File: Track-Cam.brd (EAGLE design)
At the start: 65 x 56 mm, 40 parts, among them IC1 STM32F042KT/M, IC2 BD6211F/M, IC3 BD6211F/M, X1 RASPI_BOARD_B+#_HC

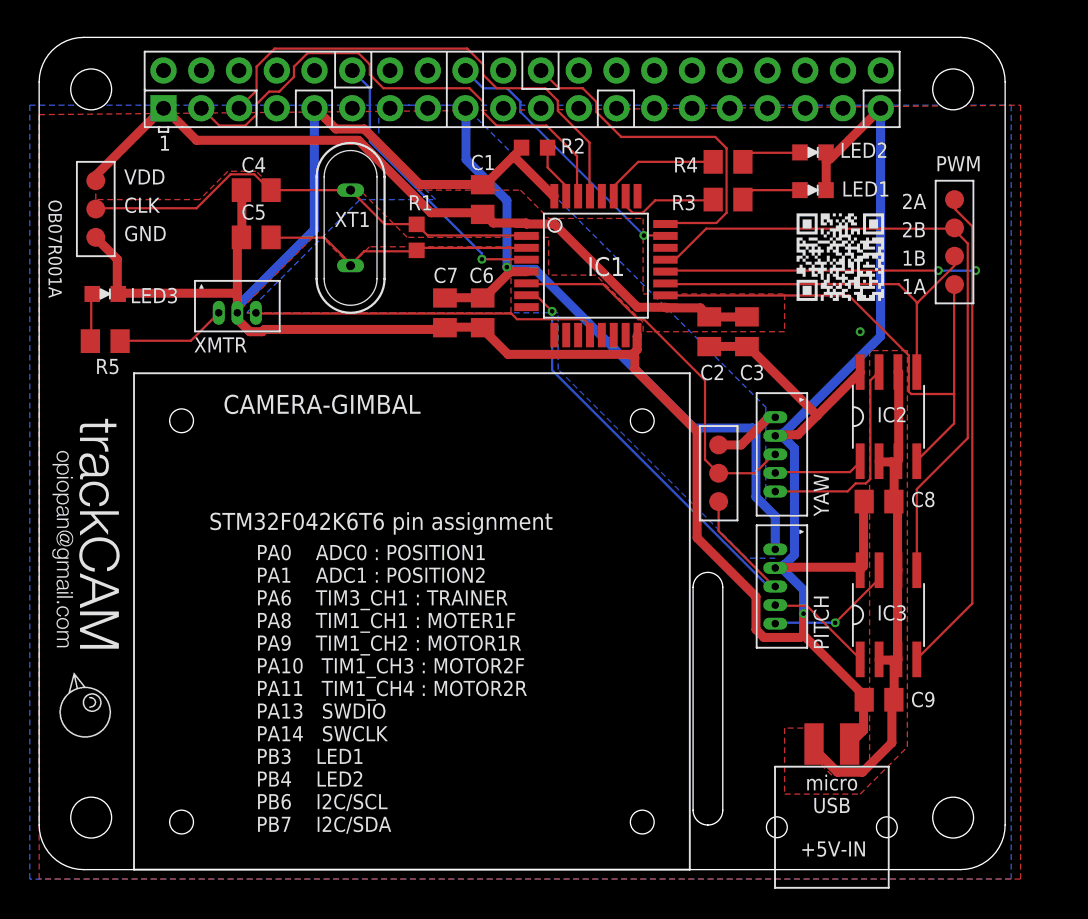
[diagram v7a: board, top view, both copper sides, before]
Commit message: add via holes for  noise immunity
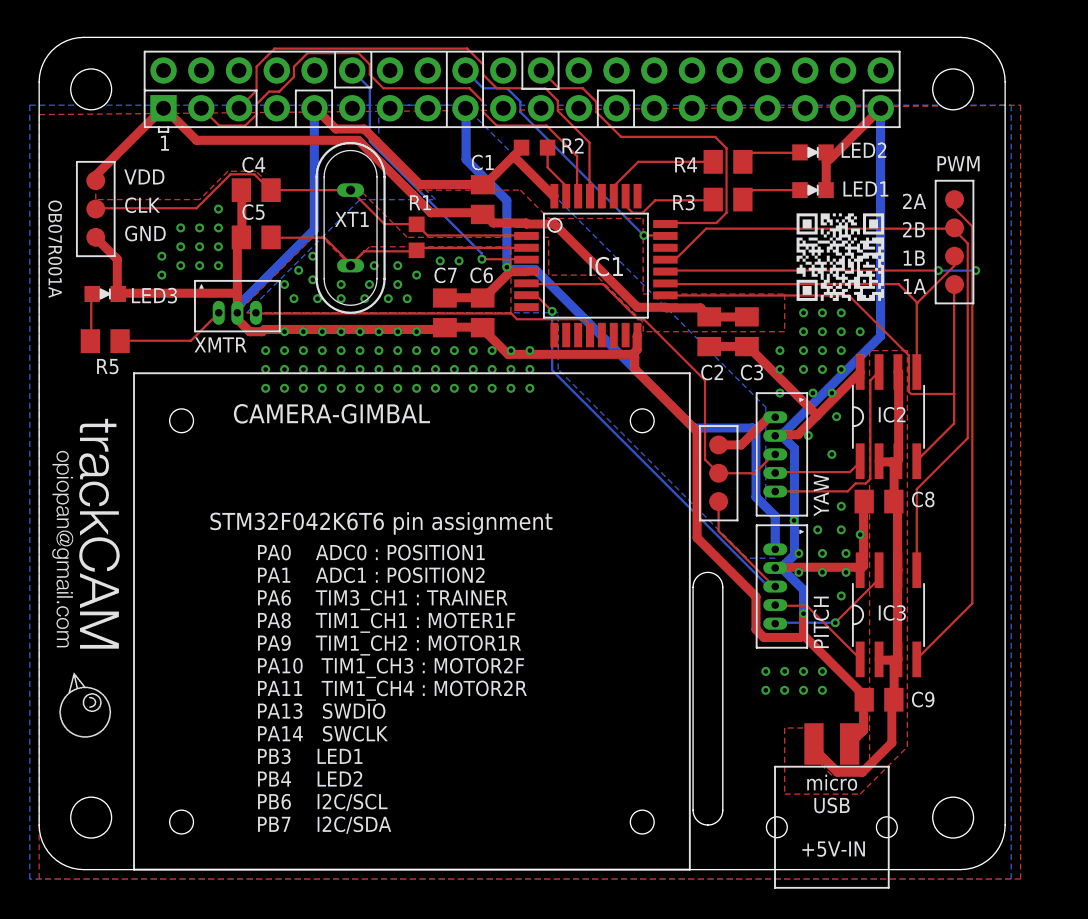
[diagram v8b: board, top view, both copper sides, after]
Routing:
- net GND: vias 2 -> 107
- net +3V3: vias 1 -> 19
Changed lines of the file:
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@@
 <setting verticaltext="up"/>
 </settings>
-<grid distance="25" unitdist="mil" unit="mil" style="lines" multiple="1" display="yes" altdistance="8" altunitdist="mil" altunit="mil"/>
+<grid distance="25" unitdist="mil" unit="mil" style="lines" multiple="1" display="no" altdistance="12.5" altunitdist="mil" altunit="mil"/>
 <layers>
 <layer number="1" name="Top" color="4" fill="1" visible="yes" active="yes"/>
@@
 <attribute name="VALUE" x="25.405" y="38.465" size="1.016" layer="27" rot="R270"/>
 </element>
-<element name="CAMERA-GIMBAL" library="mech" package="SG90-CAMERA-MOUNT-NR" value="SG-90-CAMERA-MOUNT/NR" x="25.0825" y="16.7005"/>
+<element name="CAMERA-GIMBAL" library="mech" package="SG90-CAMERA-MOUNT-NR" value="SG-90-CAMERA-MOUNT/NR" x="25.0825" y="16.7005" smashed="yes">
+<attribute name="NAME" x="13.0175" y="30.0355" size="1.27" layer="25" font="vector"/>
+</element>
 <element name="IC1" library="stm32" package="LQFP32-M" value="STM32F042KT/M" x="37.465" y="40.64" smashed="yes" rot="R270">
 <attribute name="NAME" x="39.43" y="41.21" size="1.27" layer="25" font="vector" rot="R180"/>
@@
 <vertex x="22.86" y="51.435"/>
 </polygon>
+<via x="16.51" y="39.37" extent="1-16" drill="0.3048"/>
+<via x="17.145" y="38.4175" extent="1-16" drill="0.3048"/>
+<via x="17.4625" y="40.3225" extent="1-16" drill="0.3048"/>
+<via x="18.415" y="39.6875" extent="1-16" drill="0.3048"/>
+<via x="18.415" y="41.275" extent="1-16" drill="0.3048"/>
+<via x="18.7325" y="38.4175" extent="1-16" drill="0.3048"/>
+<via x="20.32" y="38.4175" extent="1-16" drill="0.3048"/>
+<via x="20.32" y="39.37" extent="1-16" drill="0.3048"/>
+<via x="22.225" y="39.37" extent="1-16" drill="0.3048"/>
+<via x="21.9075" y="38.4175" extent="1-16" drill="0.3048"/>
+<via x="23.495" y="38.4175" extent="1-16" drill="0.3048"/>
+<via x="24.765" y="38.4175" extent="1-16" drill="0.3048"/>
+<via x="24.13" y="39.37" extent="1-16" drill="0.3048"/>
+<via x="24.13" y="40.64" extent="1-16" drill="0.3048"/>
+<via x="22.5425" y="40.64" extent="1-16" drill="0.3048"/>
+<via x="25.4" y="40.005" extent="1-16" drill="0.3048"/>
+<via x="26.9875" y="40.9575" extent="1-16" drill="0.3048"/>
+<via x="28.2575" y="40.9575" extent="1-16" drill="0.3048"/>
 </signal>
 <signal name="BOOT0">
@@
 <vertex x="-0.635" y="-0.635"/>
 </polygon>
+<via x="53.975" y="36.195" extent="1-16" drill="0.3048"/>
+<via x="51.435" y="37.465" extent="1-16" drill="0.3048"/>
+<via x="52.705" y="37.465" extent="1-16" drill="0.3048"/>
+<via x="53.975" y="37.465" extent="1-16" drill="0.3048"/>
 <via x="55.245" y="36.195" extent="1-16" drill="0.3048"/>
+<via x="52.705" y="36.195" extent="1-16" drill="0.3048"/>
+<via x="51.435" y="36.195" extent="1-16" drill="0.3048"/>
+<via x="53.975" y="34.925" extent="1-16" drill="0.3048"/>
+<via x="53.975" y="33.655" extent="1-16" drill="0.3048"/>
+<via x="49.8475" y="32.0675" extent="1-16" drill="0.3048"/>
+<via x="53.6575" y="30.48" extent="1-16" drill="0.3048"/>
+<via x="53.34" y="32.0675" extent="1-16" drill="0.3048"/>
+<via x="52.07" y="32.0675" extent="1-16" drill="0.3048"/>
+<via x="52.705" y="33.655" extent="1-16" drill="0.3048"/>
+<via x="52.705" y="34.925" extent="1-16" drill="0.3048"/>
+<via x="51.435" y="34.925" extent="1-16" drill="0.3048"/>
+<via x="51.435" y="33.655" extent="1-16" drill="0.3048"/>
+<via x="49.8475" y="33.655" extent="1-16" drill="0.3048"/>
+<via x="49.8475" y="34.925" extent="1-16" drill="0.3048"/>
+<via x="51.7525" y="29.21" extent="1-16" drill="0.3048"/>
+<via x="53.34" y="27.94" extent="1-16" drill="0.3048"/>
+<via x="53.975" y="24.4475" extent="1-16" drill="0.3048"/>
+<via x="50.8" y="23.495" extent="1-16" drill="0.3048"/>
+<via x="52.3875" y="22.86" extent="1-16" drill="0.3048"/>
+<via x="53.975" y="22.86" extent="1-16" drill="0.3048"/>
+<via x="55.245" y="22.5425" extent="1-16" drill="0.3048"/>
+<via x="54.2925" y="21.2725" extent="1-16" drill="0.3048"/>
+<via x="52.705" y="21.2725" extent="1-16" drill="0.3048"/>
+<via x="51.1175" y="21.2725" extent="1-16" drill="0.3048"/>
+<via x="54.2925" y="20.0025" extent="1-16" drill="0.3048"/>
+<via x="52.705" y="20.0025" extent="1-16" drill="0.3048"/>
+<via x="51.1175" y="20.0025" extent="1-16" drill="0.3048"/>
+<via x="53.975" y="18.415" extent="1-16" drill="0.3048"/>
+<via x="12.065" y="44.45" extent="1-16" drill="0.3048"/>
+<via x="12.065" y="43.18" extent="1-16" drill="0.3048"/>
+<via x="10.795" y="43.18" extent="1-16" drill="0.3048"/>
+<via x="9.525" y="43.18" extent="1-16" drill="0.3048"/>
+<via x="9.525" y="41.91" extent="1-16" drill="0.3048"/>
+<via x="8.255" y="41.275" extent="1-16" drill="0.3048"/>
+<via x="8.255" y="40.005" extent="1-16" drill="0.3048"/>
+<via x="9.525" y="40.64" extent="1-16" drill="0.3048"/>
+<via x="10.795" y="40.64" extent="1-16" drill="0.3048"/>
+<via x="12.065" y="40.64" extent="1-16" drill="0.3048"/>
+<via x="12.065" y="41.91" extent="1-16" drill="0.3048"/>
+<via x="10.795" y="41.91" extent="1-16" drill="0.3048"/>
+<via x="16.51" y="36.195" extent="1-16" drill="0.3048"/>
+<via x="17.78" y="36.195" extent="1-16" drill="0.3048"/>
+<via x="19.05" y="36.195" extent="1-16" drill="0.3048"/>
+<via x="20.32" y="36.195" extent="1-16" drill="0.3048"/>
+<via x="21.59" y="36.195" extent="1-16" drill="0.3048"/>
+<via x="22.86" y="36.195" extent="1-16" drill="0.3048"/>
+<via x="24.13" y="36.195" extent="1-16" drill="0.3048"/>
+<via x="25.4" y="36.195" extent="1-16" drill="0.3048"/>
+<via x="15.24" y="34.925" extent="1-16" drill="0.3048"/>
+<via x="16.51" y="34.925" extent="1-16" drill="0.3048"/>
+<via x="17.78" y="34.925" extent="1-16" drill="0.3048"/>
+<via x="19.05" y="34.925" extent="1-16" drill="0.3048"/>
+<via x="20.32" y="34.925" extent="1-16" drill="0.3048"/>
+<via x="21.59" y="34.925" extent="1-16" drill="0.3048"/>
+<via x="22.86" y="34.925" extent="1-16" drill="0.3048"/>
+<via x="24.13" y="34.925" extent="1-16" drill="0.3048"/>
+<via x="25.4" y="34.925" extent="1-16" drill="0.3048"/>
+<via x="26.67" y="34.925" extent="1-16" drill="0.3048"/>
+<via x="27.94" y="34.925" extent="1-16" drill="0.3048"/>
+<via x="29.21" y="34.925" extent="1-16" drill="0.3048"/>
+<via x="30.48" y="34.925" extent="1-16" drill="0.3048"/>
+<via x="31.75" y="34.925" extent="1-16" drill="0.3048"/>
+<via x="33.02" y="34.925" extent="1-16" drill="0.3048"/>
+<via x="33.02" y="33.655" extent="1-16" drill="0.3048"/>
+<via x="31.75" y="33.655" extent="1-16" drill="0.3048"/>
+<via x="30.48" y="33.655" extent="1-16" drill="0.3048"/>
+<via x="29.21" y="33.655" extent="1-16" drill="0.3048"/>
+<via x="27.94" y="33.655" extent="1-16" drill="0.3048"/>
+<via x="26.67" y="33.655" extent="1-16" drill="0.3048"/>
+<via x="25.4" y="33.655" extent="1-16" drill="0.3048"/>
+<via x="24.13" y="33.655" extent="1-16" drill="0.3048"/>
+<via x="22.86" y="33.655" extent="1-16" drill="0.3048"/>
+<via x="21.59" y="33.655" extent="1-16" drill="0.3048"/>
+<via x="20.32" y="33.655" extent="1-16" drill="0.3048"/>
+<via x="19.05" y="33.655" extent="1-16" drill="0.3048"/>
+<via x="17.78" y="33.655" extent="1-16" drill="0.3048"/>
+<via x="16.51" y="33.655" extent="1-16" drill="0.3048"/>
+<via x="15.24" y="33.655" extent="1-16" drill="0.3048"/>
+<via x="15.24" y="32.385" extent="1-16" drill="0.3048"/>
+<via x="16.51" y="32.385" extent="1-16" drill="0.3048"/>
+<via x="17.78" y="32.385" extent="1-16" drill="0.3048"/>
+<via x="19.05" y="32.385" extent="1-16" drill="0.3048"/>
+<via x="20.32" y="32.385" extent="1-16" drill="0.3048"/>
+<via x="21.59" y="32.385" extent="1-16" drill="0.3048"/>
+<via x="22.86" y="32.385" extent="1-16" drill="0.3048"/>
+<via x="24.13" y="32.385" extent="1-16" drill="0.3048"/>
+<via x="25.4" y="32.385" extent="1-16" drill="0.3048"/>
+<via x="26.67" y="32.385" extent="1-16" drill="0.3048"/>
+<via x="27.94" y="32.385" extent="1-16" drill="0.3048"/>
+<via x="29.21" y="32.385" extent="1-16" drill="0.3048"/>
+<via x="30.48" y="32.385" extent="1-16" drill="0.3048"/>
+<via x="31.75" y="32.385" extent="1-16" drill="0.3048"/>
+<via x="33.02" y="32.385" extent="1-16" drill="0.3048"/>
+<via x="48.895" y="13.335" extent="1-16" drill="0.3048"/>
+<via x="50.165" y="13.335" extent="1-16" drill="0.3048"/>
+<via x="51.435" y="13.335" extent="1-16" drill="0.3048"/>
+<via x="52.705" y="13.335" extent="1-16" drill="0.3048"/>
+<via x="52.705" y="12.065" extent="1-16" drill="0.3048"/>
+<via x="51.435" y="12.065" extent="1-16" drill="0.3048"/>
+<via x="50.165" y="12.065" extent="1-16" drill="0.3048"/>
+<via x="48.895" y="12.065" extent="1-16" drill="0.3048"/>
 </signal>
 <signal name="MOTOR2_POS">
